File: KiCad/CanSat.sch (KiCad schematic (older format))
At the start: 0 parts

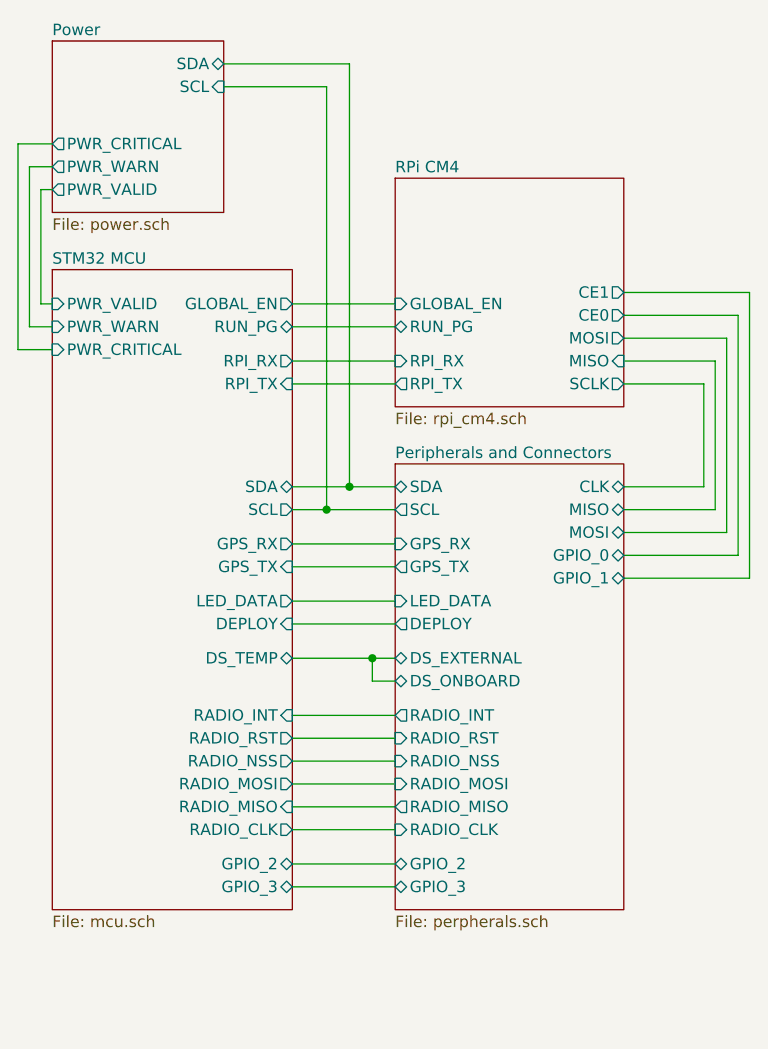
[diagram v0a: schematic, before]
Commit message: Added a button and a buzzer
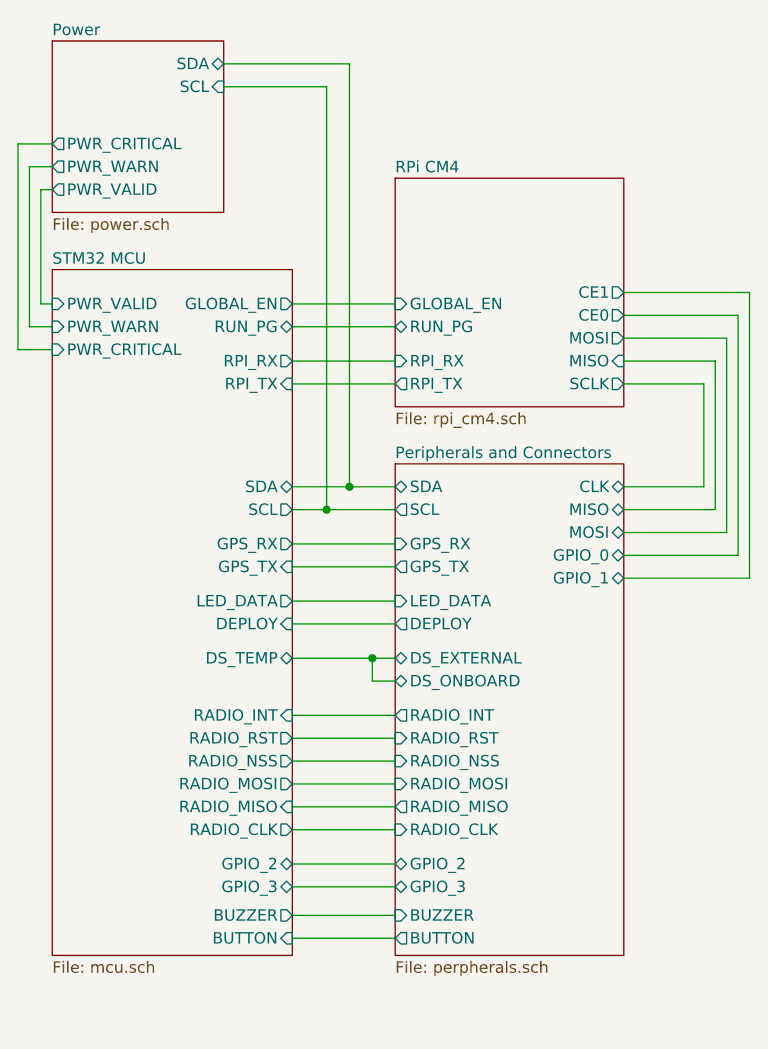
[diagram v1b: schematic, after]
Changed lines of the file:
@@
 	3500 3000 3050 3000
 $Sheet
-S 2000 2500 1050 2800
+S 2000 2500 1050 3000
 U 5FCA62D1
 F0 "STM32 MCU" 50
@@
 F22 "GPIO_2" B R 3050 5100 50
 F23 "GPIO_3" B R 3050 5200 50
+F24 "BUZZER" O R 3050 5325 50
+F25 "BUTTON" I R 3050 5425 50
 $EndSheet
 Wire Wire Line
@@
 $EndSheet
 $Sheet
-S 3500 3350 1000 1950
+S 3500 3350 1000 2150
 U 5FCA658C
 F0 "Peripherals and Connectors" 50
@@
 F21 "GPIO_2" B L 3500 5100 50
 F22 "GPIO_3" B L 3500 5200 50
+F23 "BUZZER" I L 3500 5325 50
+F24 "BUTTON" O L 3500 5425 50
 $EndSheet
+Wire Wire Line
+	3500 5325 3050 5325
+Wire Wire Line
+	3500 5425 3050 5425
 $EndSCHEMATC

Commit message: Dirty production PCBs commit
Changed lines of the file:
@@
 	3500 3000 3050 3000
 $Sheet
-S 2000 2500 1050 3000
+S 2000 2500 1050 3225
 U 5FCA62D1
 F0 "STM32 MCU" 50
@@
 F24 "BUZZER" O R 3050 5325 50
 F25 "BUTTON" I R 3050 5425 50
+F26 "ACC_INT2" I R 3050 5650 50
+F27 "ACC_INT1" I R 3050 5550 50
 $EndSheet
 Wire Wire Line
@@
 F10 "CE1" O R 4500 2600 50
 $EndSheet
+Wire Wire Line
+	3500 5325 3050 5325
+Wire Wire Line
+	3500 5425 3050 5425
 $Sheet
-S 3500 3350 1000 2150
+S 3500 3350 1000 2375
 U 5FCA658C
 F0 "Peripherals and Connectors" 50
@@
 F23 "BUZZER" I L 3500 5325 50
 F24 "BUTTON" O L 3500 5425 50
+F25 "ACC_INT1" O L 3500 5550 50
+F26 "ACC_INT2" O L 3500 5650 50
 $EndSheet
 Wire Wire Line
-	3500 5325 3050 5325
+	3050 5550 3500 5550
 Wire Wire Line
-	3500 5425 3050 5425
+	3500 5650 3050 5650
 $EndSCHEMATC
